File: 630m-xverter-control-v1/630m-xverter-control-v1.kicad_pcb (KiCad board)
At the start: 2 copper layers, 126.4 x 69.8 mm, 53 parts, among them J1 Rig Transverter, J2 ALC, J3 ANT, J4 TX_TO_AMP, J5 TX_FROM_AMP, J6 Power, J7 TX AMP POWER, K1 DS1E-M-DC12V, K2 DS1E-M-DC12V, K3 DS1E-M-DC12V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

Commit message: Update PCB layout, it should work? kinda? we'll see.
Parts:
- moved C7 26.9 mm to (95.1, 29.8)
- moved Q6 26.9 mm to (91.6, 59.1)
- moved Q7 26.9 mm to (87.4, 19.0)
- moved R12 26.9 mm to (92.6, 73.9)
- moved R13 26.9 mm to (84.9, 24.8)
- moved C8 26.9 mm to (99.1, 50.2)
- moved C9 26.9 mm to (91.0, 45.1)
- moved H1 26.9 mm to (104.6, 75.5)
- moved H4 26.9 mm to (104.6, 19.6)
- moved J2 26.9 mm to (104.6, 58.4)
- moved J6 26.9 mm to (104.6, 45.0)
- moved J7 26.9 mm to (104.6, 29.8)
- moved R11 26.9 mm to (88.5, 66.2)
- moved Q3 2.33 mm to (81.8, 75.8), turned to 180 degrees
- moved Q2 2.08 mm to (77.5, 47.0)
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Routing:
- net XVERTER_ALC_INPUT: track 3.35 -> 90.1 mm, vias 0 -> 1
- net PA_DISABLE: track 119.6 -> 200.1 mm, vias 0 -> 1
- net TX_ENABLE: track 0.00 -> 55.0 mm
- net Net-(D7-Pad2): track 5.27 -> 56.5 mm
- net Net-(D6-Pad2): track 5.19 -> 56.0 mm
- net Net-(Q4-Pad2): track 0.00 -> 45.3 mm
- net XVERTER_TX_PA_DISABLE: track 3.35 -> 43.4 mm
- net Net-(D5-Pad2): track 5.08 -> 30.7 mm
- net Net-(Q3-Pad2): track 0.00 -> 10.6 mm
- net Net-(Q2-Pad2): track 0.00 -> 7.48 mm
- net Net-(Q1-Pad2): track 0.00 -> 7.43 mm
- added copper zone on B.Cu, net GND
- added copper zone on F.Cu, net GND
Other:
- board size 126.4 x 69.8 mm -> 100 x 71 mm

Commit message: Whoops - my coil orientation/pinout was JUST PLAIN WRONG.
So fix the schematic to do the right thing; I'll have to hack something on my
development pcb to test that the filter actually works..
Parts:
- turned L1 to 90 degrees
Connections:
- C2 pad 1: Net-(C2-Pad1) -> Net-(C1-Pad2)
- L1 pad 1: Net-(C1-Pad1) -> RX_FILT_IN
- L1 pad 6: RX_FILT_IN -> Net-(C1-Pad1)
- L2 pad 1: Net-(C1-Pad2) -> Net-(L2-Pad1)
- L2 pad 6: Net-(C2-Pad1) -> Net-(C1-Pad2)
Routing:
- net Net-(C2-Pad1): track 20.6 -> 0.00 mm
- net Net-(C1-Pad2): track 7.62 -> 28.2 mm
- net Net-(C1-Pad1): track 18.4 -> 11.6 mm
- net RX_FILT_IN: track 42.3 -> 46.1 mm

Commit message: more fixes:
* missed ground plane ties for the signal connectors, whoops
* add ground pins for the coils so they can be tied to ground
* add label
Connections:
- J3 pad 2: Net-(J3-Pad2) -> GND
- J4 pad 2: Net-(J4-Pad2) -> GND
- J5 pad 2: Net-(J5-Pad2) -> GND
- L1 pad 7: (no net) -> GND
- L1 pad 8: (no net) -> GND
- L2 pad 3: GND -> Net-(L2-Pad3)
- L2 pad 4: Net-(L2-Pad4) -> GND
- L2 pad 7: (no net) -> GND
- L2 pad 8: (no net) -> GND
- L3 pad 7: (no net) -> GND
- L3 pad 8: (no net) -> GND
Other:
- board text added: "630m ctrl board Dec 2020 v0.3 Adrian Chadd KK6VQK"

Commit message: More v0.3 fixes -
* fix the bloody signal routing for that middle IF coil, what was I thinking
* don't use a cap to xverter-gnd; just tie them together and to ground

That should be much better!
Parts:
- removed C4: 0.1uF, Capacitor_THT:C_Disc_D5.0mm_W2.5mm_P5.00mm
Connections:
- C3 pad 2: GND -> XVERTER_EARTH
- C5 pad 2: GND -> XVERTER_EARTH
- C6 pad 2: GND -> XVERTER_EARTH
- C7 pad 2: GND -> XVERTER_EARTH
- C8 pad 1: GND -> XVERTER_EARTH
- C9 pad 2: GND -> XVERTER_EARTH
- D1 pad 2: GND -> XVERTER_EARTH
- D2 pad 1: GND -> XVERTER_EARTH
- D3 pad 1: GND -> XVERTER_EARTH
- D4 pad 1: GND -> XVERTER_EARTH
- H1 pad 1: GND -> XVERTER_EARTH
- H2 pad 1: GND -> XVERTER_EARTH
- H3 pad 1: GND -> XVERTER_EARTH
- H4 pad 1: GND -> XVERTER_EARTH
- J2 pad 2: GND -> XVERTER_EARTH
- J3 pad 2: GND -> XVERTER_EARTH
- J4 pad 2: GND -> XVERTER_EARTH
- J5 pad 2: GND -> XVERTER_EARTH
- J6 pad 2: GND -> XVERTER_EARTH
- J7 pad 2: GND -> XVERTER_EARTH
- K2 pad 12: GND -> XVERTER_EARTH
- L1 pad 3: GND -> XVERTER_EARTH
- L1 pad 4: GND -> XVERTER_EARTH
- L1 pad 7: GND -> XVERTER_EARTH
- L1 pad 8: GND -> XVERTER_EARTH
- L2 pad 4: GND -> XVERTER_EARTH
- L2 pad 7: GND -> XVERTER_EARTH
- L2 pad 8: GND -> XVERTER_EARTH
- L3 pad 3: GND -> XVERTER_EARTH
- L3 pad 4: GND -> XVERTER_EARTH
- L3 pad 7: GND -> XVERTER_EARTH
- L3 pad 8: GND -> XVERTER_EARTH
- Q1 pad 1: GND -> XVERTER_EARTH
- Q2 pad 1: GND -> XVERTER_EARTH
- Q3 pad 1: GND -> XVERTER_EARTH
- Q4 pad 1: GND -> XVERTER_EARTH
- Q6 pad 1: GND -> XVERTER_EARTH
- R10 pad 2: GND -> XVERTER_EARTH
- R12 pad 2: GND -> XVERTER_EARTH
- R2 pad 2: GND -> XVERTER_EARTH
- R4 pad 2: GND -> XVERTER_EARTH
- R6 pad 2: GND -> XVERTER_EARTH
- R8 pad 2: GND -> XVERTER_EARTH
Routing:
- net Net-(C1-Pad2): track 28.2 -> 39.5 mm
- net XVERTER_EARTH: track 4.10 -> 0.72 mm
- net RX_FILT_IN: track 46.1 -> 45.1 mm
- added copper zone on B.Cu, net XVERTER_EARTH
- added copper zone on F.Cu, net XVERTER_EARTH

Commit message: * More layout fixes * Make the silk screen layer not actually terrible
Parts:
- H1, H2, H3, H4: footprint MountingHole:MountingHole_4.3x6.2mm_M4_Pad_Via -> MountingHole:MountingHole_4.3mm_M4_Pad_Via
- L1, L2, L3: value coilcraft_slot10 -> 455KHz IF
- moved R4 1.32 mm to (75.9, 51.3)
- moved R3 1.32 mm to (79.0, 51.3)
- renumbered D4 to SP1, D3 to SP2
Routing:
- net PA_DISABLE: track 200.1 -> 205.7 mm
- net TX_ENABLE: track 55.0 -> 57.9 mm
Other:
- board text added: "ALC"
- board text added: "ALC input"
- board text added: "ANT"
- board text added: "GND"
- board text added: "PA_DIS"
- board text added: "PTT"
- board text added: "Power Input"
- board text added: "RX_IN"
- board text added: "RX_OUT"
- board text added: "TX"
- board text added: "TX Amp Power Out"
- board text added: "TX FROM AMP"
- board text added: "TX TO AMP"
- board text added: "VCC"

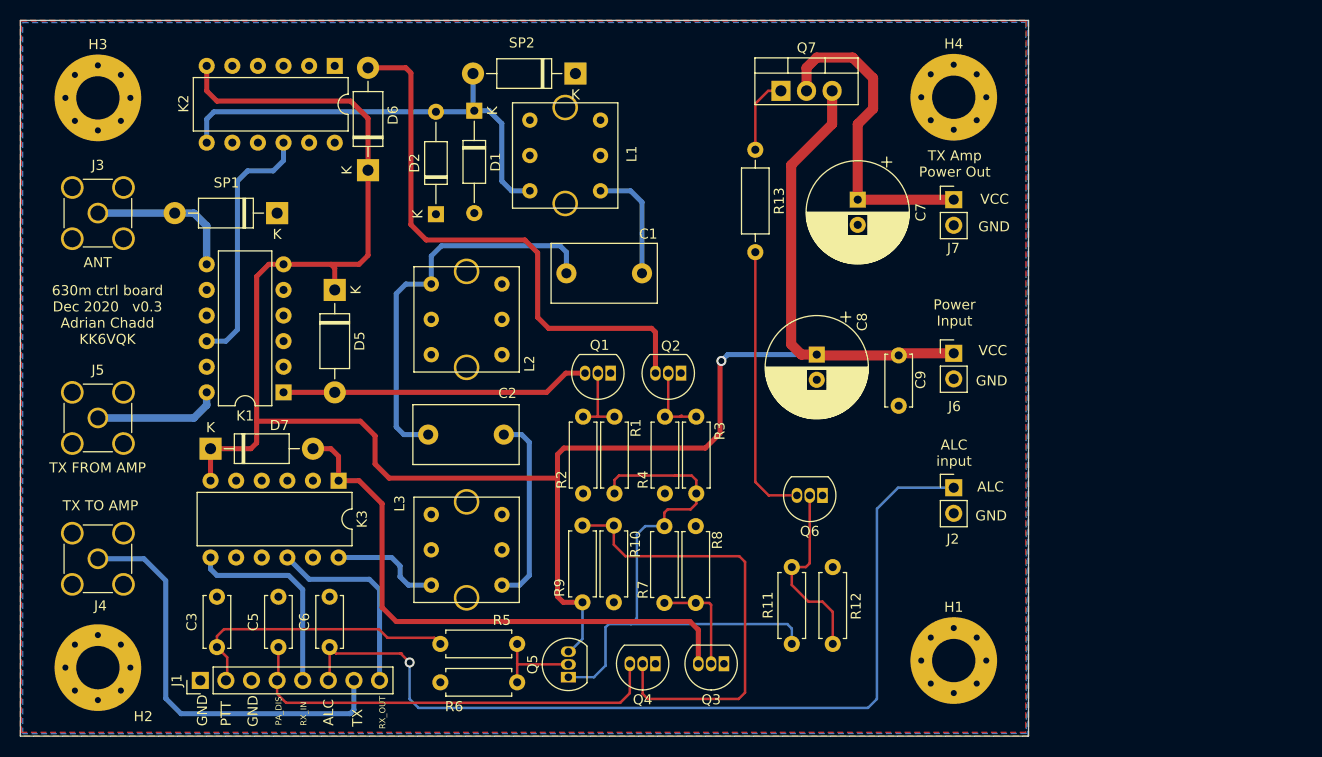
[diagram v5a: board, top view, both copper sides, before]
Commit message: I got the fucking relay power backwards. WTAF.
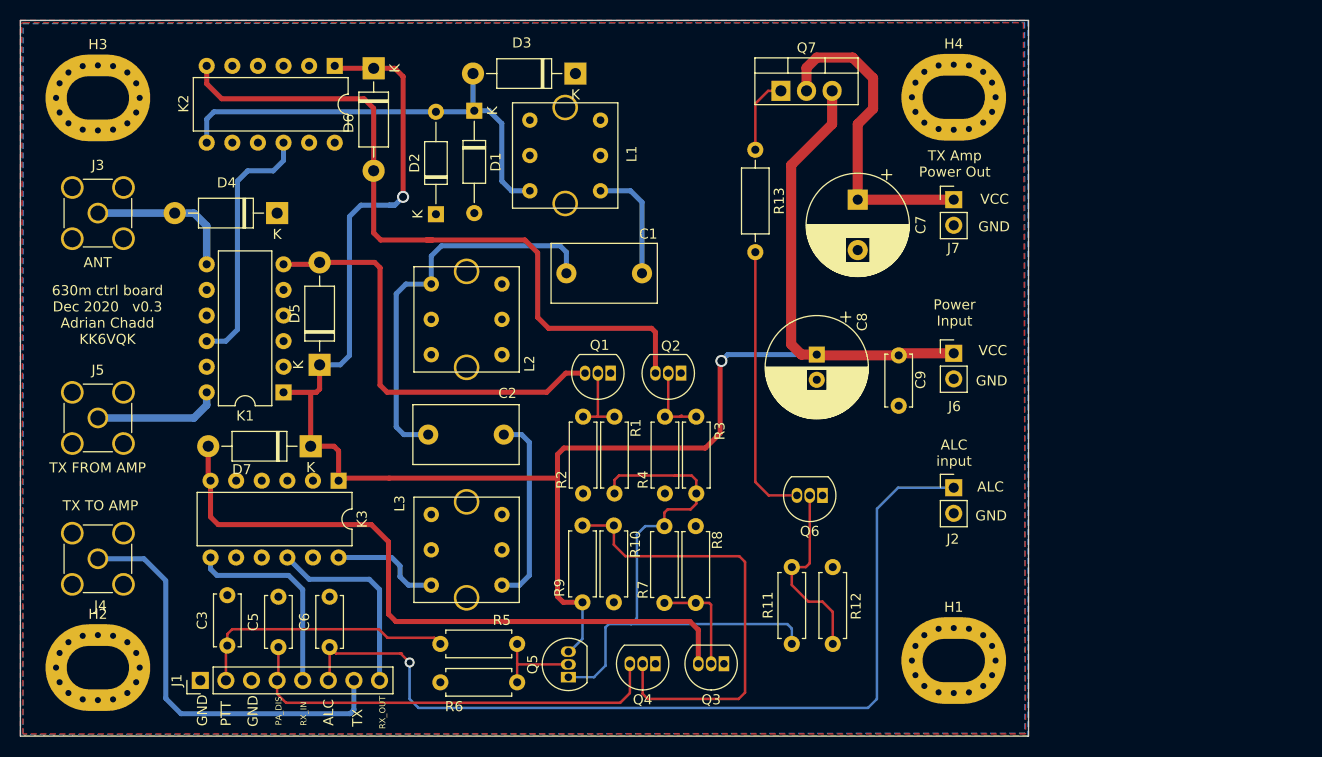
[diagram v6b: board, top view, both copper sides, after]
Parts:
- C7: footprint Capacitor_THT:CP_Radial_D10.0mm_P2.50mm -> Capacitor_THT:CP_Radial_D10.0mm_P5.00mm
- H1, H2, H3, H4: footprint MountingHole:MountingHole_4.3mm_M4_Pad_Via -> MountingHole:MountingHole_4.3x6.2mm_M4_Pad_Via
- L1, L2, L3: value 455KHz IF -> coilcraft_slot10
- R1, R11, R3, R5, R7: value R -> 1K
- R12, R2, R4, R6, R8: value R -> 10K
- moved D6 10.1 mm to (47.0, 16.8), turned to 270 degrees
- moved D7 9.93 mm to (40.8, 54.2), turned to 180 degrees
- moved D5 7.58 mm to (41.7, 46.2), turned to 90 degrees
- moved C3 1.04 mm to (32.5, 74.0)
- renumbered SP2 to D3, SP1 to D4
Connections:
- K1 pad 1: Net-(D5-Pad2) -> PA_DISABLE
- K1 pad 6: PA_DISABLE -> Net-(D5-Pad2)
- K2 pad 1: Net-(D6-Pad2) -> PA_DISABLE
- K2 pad 6: PA_DISABLE -> Net-(D6-Pad2)
- K3 pad 1: Net-(D7-Pad2) -> PA_DISABLE
- K3 pad 6: PA_DISABLE -> Net-(D7-Pad2)
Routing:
- net PA_DISABLE: track 205.7 -> 181.5 mm, vias 1 -> 2
- net Net-(D6-Pad2): track 56.0 -> 72.2 mm
- net Net-(D5-Pad2): track 30.7 -> 42.9 mm
- net Net-(D7-Pad2): track 56.5 -> 67.7 mm
- net XVERTER_PTT: track 27.9 -> 26.8 mm
